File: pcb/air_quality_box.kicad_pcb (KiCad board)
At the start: 2 copper layers, 10 parts, among them J1 MH-Z19B, J2 Conn_01x06_Female, J3 Conn_01x05_Male, J4 Conn_01x09_Female, SW1 SW_SPDT, U1 NodeMCU_ESP8266

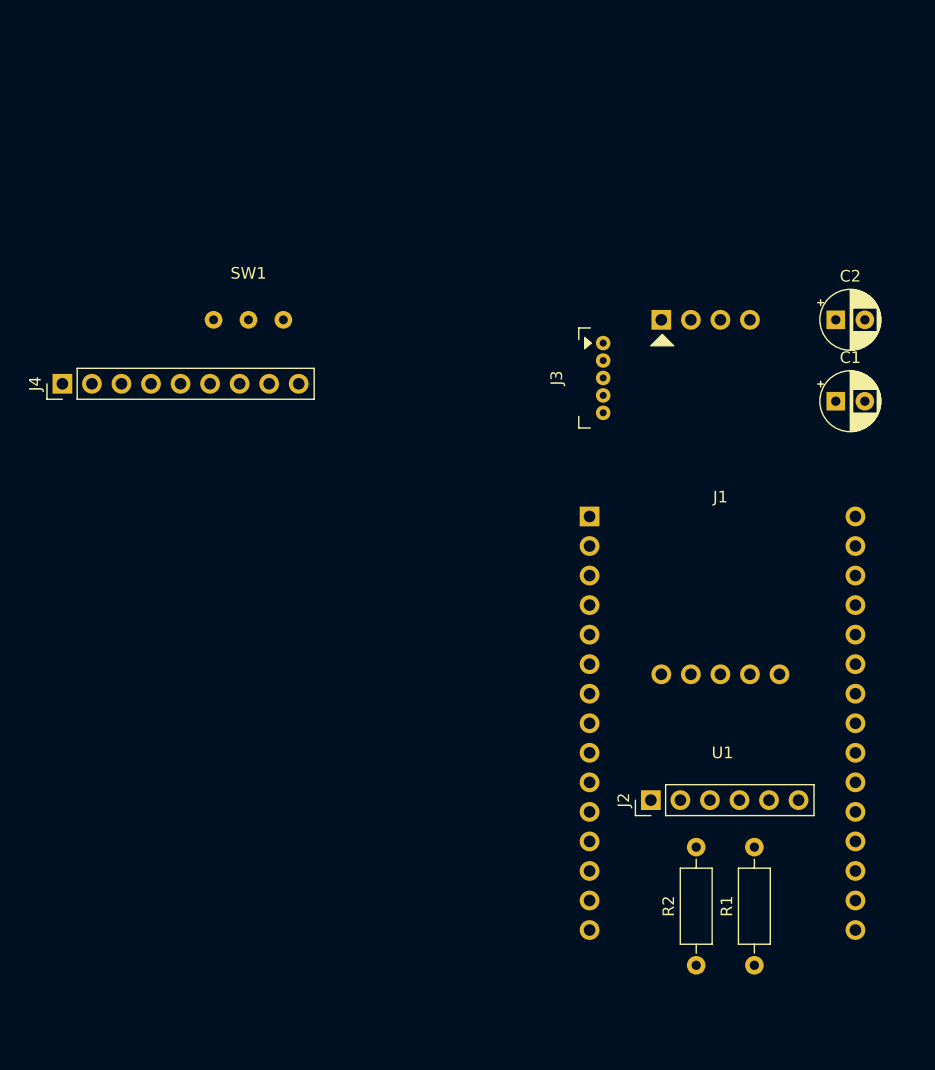
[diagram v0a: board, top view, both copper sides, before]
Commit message: Create basic board layout
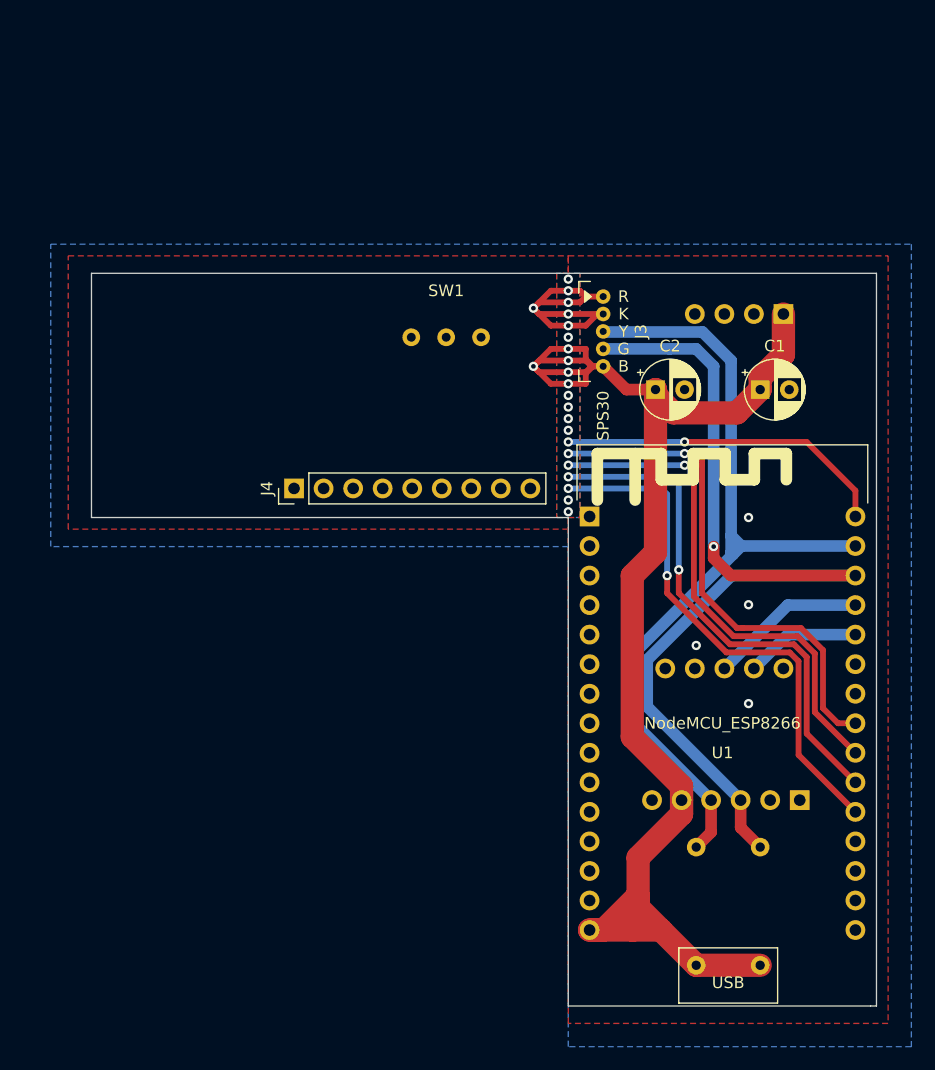
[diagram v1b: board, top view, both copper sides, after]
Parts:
- J1, R1, R2: moved to B.Cu
- J2: value Conn_01x06_Female -> BME680; moved to B.Cu
- J3: value Conn_01x05_Male -> SPS30
- J4: value Conn_01x09_Female -> ST7565
- moved J4 21.9 mm to (115.9, 62.0)
- moved SW1 17.1 mm to (129.0, 49.0)
- moved C2 16.6 mm to (147.0, 53.5)
- moved J2 12.8 mm to (159.4, 88.8)
- moved C1 6.58 mm to (156.0, 53.5)
- moved R2 5.50 mm to (156.0, 103.0)
- moved R1 5.00 mm to (150.5, 103.0)
- moved J3 4.00 mm to (142.5, 48.5)
- moved J1 0.60 mm to (152.9, 62.2), turned to 180 degrees
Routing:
- net +5V: track 0.00 -> 126.0 mm, vias 0 -> 5
- net I2C_SDA: track 0.00 -> 80.5 mm, vias 0 -> 1
- net I2C_SCL: track 0.00 -> 72.9 mm
- net LCD_CS: track 0.00 -> 45.9 mm, vias 0 -> 2
- net LCD_DC: track 0.00 -> 45.0 mm, vias 0 -> 2
- net SPI_MOSI: track 0.00 -> 44.3 mm, vias 0 -> 2
- net SPI_SCL: track 0.00 -> 44.0 mm, vias 0 -> 2
- net LCD_RST: track 0.00 -> 28.6 mm, vias 0 -> 2
- net GND: track 0.00 -> 25.0 mm, vias 0 -> 9
- net UART_1_RX: track 0.00 -> 13.5 mm
- net UART_1_TX: track 0.00 -> 9.94 mm
- net (no net): vias 0 -> 8
- added copper zone on B.Cu, net GND
- added copper zone on F.Cu, net GND
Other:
- board outline added: 67.5 x 63 mm
- board text added: "B"
- board text added: "G"
- board text added: "K"
- board text added: "R"
- board text added: "USB"
- board text added: "Y"

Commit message: Position the LCD in the center of the board
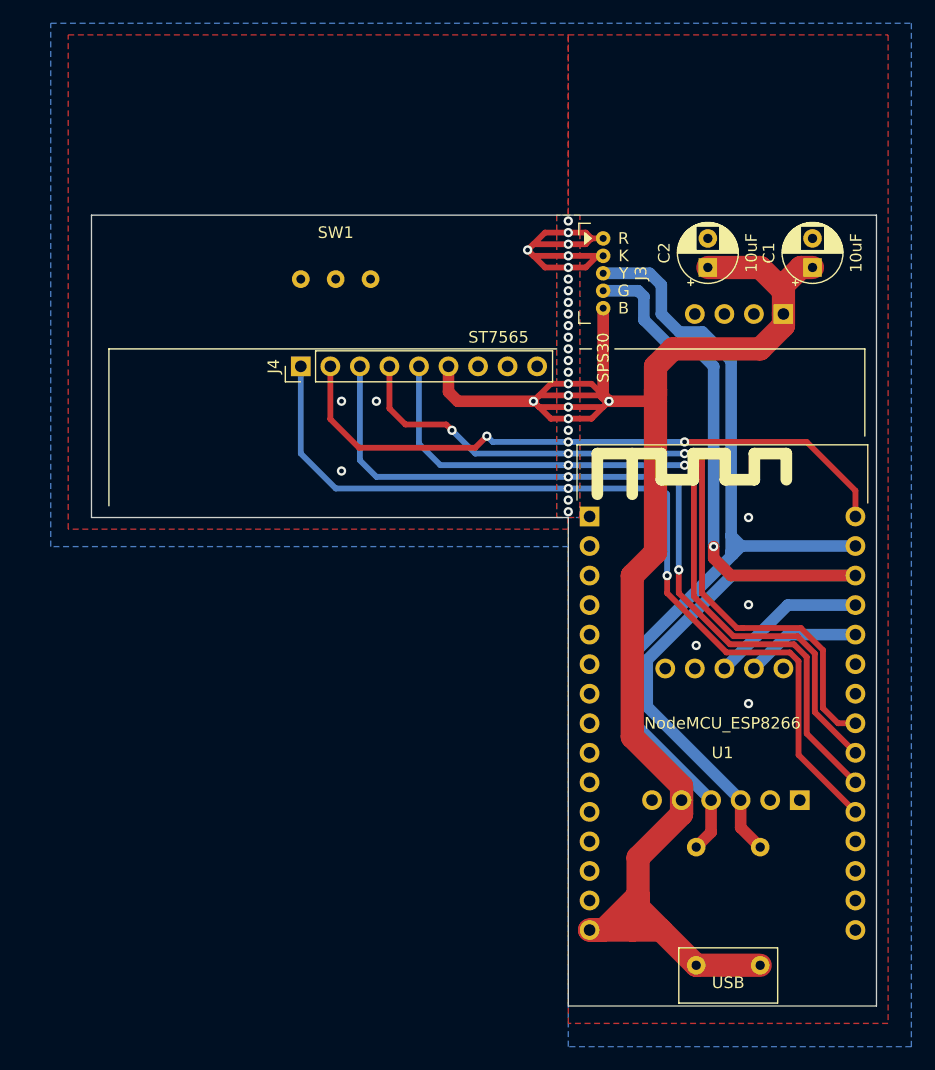
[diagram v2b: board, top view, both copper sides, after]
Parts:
- moved C1 11.4 mm to (160.5, 43.0), turned to 90 degrees
- moved C2 11.4 mm to (151.5, 43.0), turned to 90 degrees
- moved SW1 10.7 mm to (119.5, 44.0)
- moved J4 10.5 mm to (116.5, 51.5)
- moved J3 5.00 mm to (142.5, 43.5)
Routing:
- net LCD_CS: track 45.9 -> 77.7 mm
- net +5V: track 126.0 -> 155.4 mm, vias 5 -> 6
- net LCD_RST: track 28.6 -> 55.3 mm, vias 2 -> 3
- net LCD_DC: track 45.0 -> 71.6 mm
- net SPI_SCL: track 44.0 -> 64.6 mm, vias 2 -> 3
- net SPI_MOSI: track 44.3 -> 64.6 mm
- net I2C_SCL: track 72.9 -> 76.4 mm
- net I2C_SDA: track 80.5 -> 83.7 mm
- net GND: track 25.0 -> 27.0 mm, vias 9 -> 12
- net (no net): vias 8 -> 13
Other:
- board size 67.5 x 63 mm -> 67.5 x 68 mm

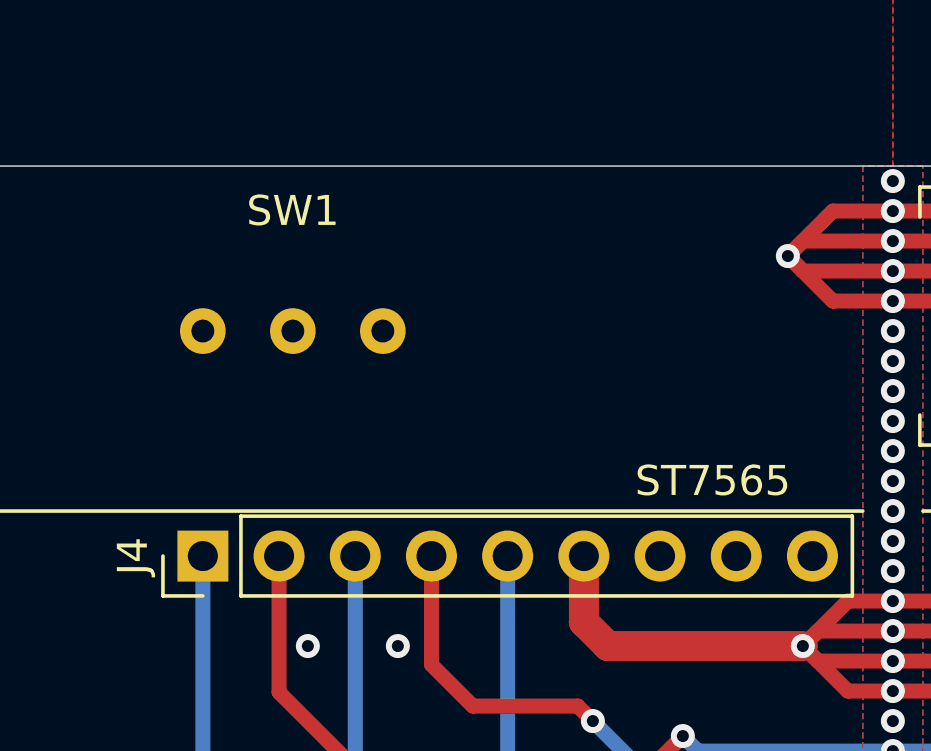
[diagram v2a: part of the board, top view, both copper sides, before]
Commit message: Add JCL order number location to board
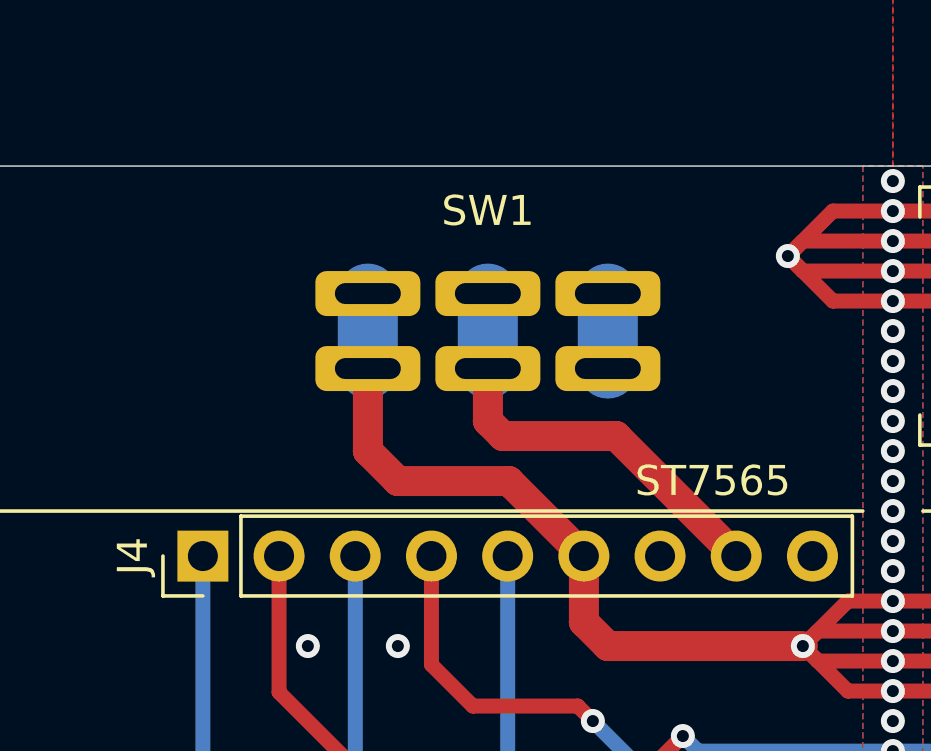
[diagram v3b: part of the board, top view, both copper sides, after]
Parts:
- moved SW1 6.50 mm to (126.0, 44.0)
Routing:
- net Net-(J4-Pad8): track 0.00 -> 14.4 mm
- net +5V: track 155.4 -> 169.3 mm
- net Net-(SW1-Pad1): track 0.00 -> 2.50 mm
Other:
- board text added: "JLCJLCJLCJLC"
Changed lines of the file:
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@@
   (general
     (thickness 1.6)
-    (drawings 58)
-    (tracks 217)
+    (drawings 59)
+    (tracks 228)
     (zones 0)
     (modules 10)
@@
   )
   (setup
-    (last_trace_width 0.5)
+    (last_trace_width 2)
     (user_trace_width 0.5)
     (user_trace_width 1)
@@
       (outputformat 1)
       (mirror false)
-      (drillshape 1)
+      (drillshape 0)
       (scaleselection 1)
       (outputdirectory ""))
@@
     (add_net UART_1_RX)
     (add_net UART_1_TX)
+  )
+  (module air_quality_box:switch (layer F.Cu)
+    (at 126 44 180)
+    (fp_text reference SW1 (at 0 4) (layer F.SilkS)
+      (effects (font (size 1 1) (thickness 0.15)))
+    )
+    (fp_text value SW_SPDT (at 0 -5) (layer F.Fab)
+      (effects (font (size 1 1) (thickness 0.15)))
+    )
+    (fp_line (start -8 0) (end -8 -4) (layer F.Fab) (width 0.12))
+    (fp_line (start -8 -4) (end 8 -4) (layer F.Fab) (width 0.12))
+    (fp_line (start 8 -4) (end 8 4) (layer F.Fab) (width 0.12))
+    (fp_line (start 8 4) (end -8 4) (layer F.Fab) (width 0.12))
+    (fp_line (start -8 4) (end -8 0) (layer F.Fab) (width 0.12))
+    (fp_line (start -8 -4) (end -12 -4) (layer F.Fab) (width 0.12))
+    (fp_line (start -12 -4) (end -12 4) (layer F.Fab) (width 0.12))
+    (fp_line (start -12 4) (end -8 4) (layer F.Fab) (width 0.12))
+    (fp_line (start 8 4) (end 12 4) (layer F.Fab) (width 0.12))
+    (fp_line (start 12 4) (end 12 -4) (layer F.Fab) (width 0.12))
+    (fp_line (start 12 -4) (end 8 -4) (layer F.Fab) (width 0.12))
+    (pad 3 thru_hole roundrect (at 4 1.25 180) (size 3.5 1.5) (drill oval 2.2 0.7) (layers *.Cu *.Mask) (roundrect_rratio 0.25)
+      (net 1 +5V))
+    (pad 2 thru_hole roundrect (at 0 1.25 180) (size 3.5 1.5) (drill oval 2.2 0.7) (layers *.Cu *.Mask) (roundrect_rratio 0.25)
+      (net 19 "Net-(J4-Pad8)"))
+    (pad 1 thru_hole roundrect (at -4 1.25 180) (size 3.5 1.5) (drill oval 2.2 0.7) (layers *.Cu *.Mask) (roundrect_rratio 0.25)
+      (net 20 "Net-(SW1-Pad1)"))
+    (pad 3 thru_hole roundrect (at 4 -1.25 180) (size 3.5 1.5) (drill oval 2.2 0.7) (layers *.Cu *.Mask) (roundrect_rratio 0.25)
+      (net 1 +5V))
+    (pad 2 thru_hole roundrect (at 0 -1.25 180) (size 3.5 1.5) (drill oval 2.2 0.7) (layers *.Cu *.Mask) (roundrect_rratio 0.25)
+      (net 19 "Net-(J4-Pad8)"))
+    (pad 1 thru_hole roundrect (at -4 -1.25 180) (size 3.5 1.5) (drill oval 2.2 0.7) (layers *.Cu *.Mask) (roundrect_rratio 0.25)
+      (net 20 "Net-(SW1-Pad1)"))
   )
   (module air_quality_box:ZH_1.5mm_5P (layer F.Cu)
@@
     )
   )
-  (module air_quality_box:switch (layer F.Cu)
-    (at 119.5 44 180)
-    (fp_text reference SW1 (at 0 4) (layer F.SilkS)
-      (effects (font (size 1 1) (thickness 0.15)))
-    )
-    (fp_text value SW_SPDT (at 0 -5) (layer F.Fab)
-      (effects (font (size 1 1) (thickness 0.15)))
-    )
-    (pad 1 thru_hole circle (at -3 0 180) (size 1.524 1.524) (drill 0.762) (layers *.Cu *.Mask)
-      (net 20 "Net-(SW1-Pad1)"))
-    (pad 2 thru_hole circle (at 0 0 180) (size 1.524 1.524) (drill 0.762) (layers *.Cu *.Mask)
-      (net 19 "Net-(J4-Pad8)"))
-    (pad 3 thru_hole circle (at 3 0 180) (size 1.524 1.524) (drill 0.762) (layers *.Cu *.Mask)
-      (net 1 +5V))
-  )
   (module air_quality_box:NodeMCU_ESP8266 (layer F.Cu)
     (at 152.760001 82.190001)
@@
     (pad 30 thru_hole circle (at 11.43 17.78) (size 1.7 1.7) (drill 1) (layers *.Cu *.Mask)
       (net 36 "Net-(U1-Pad30)"))
+  )
+  (gr_text JLCJLCJLCJLC (at 105 63) (layer B.SilkS)
+    (effects (font (size 1 1) (thickness 0.15)) (justify mirror))
   )
   (gr_line (start 165 50) (end 165 57.5) (layer F.SilkS) (width 0.12))
@@
   (segment (start 142.5 54) (end 143 54.5) (width 1) (layer F.Cu) (net 1))
   (segment (start 142.5 46.5) (end 142.5 54) (width 1) (layer F.Cu) (net 1))
+  (segment (start 129.2 51.5) (end 126.7 49) (width 1) (layer F.Cu) (net 1))
+  (segment (start 126.7 49) (end 123 49) (width 1) (layer F.Cu) (net 1))
+  (segment (start 122 48) (end 122 45.25) (width 1) (layer F.Cu) (net 1))
+  (segment (start 123 49) (end 122 48) (width 1) (layer F.Cu) (net 1))
+  (segment (start 122 42.75) (end 122 45.25) (width 2) (layer B.Cu) (net 1))
   (segment (start 139.5 40) (end 141 40) (width 0.5) (layer F.Cu) (net 2))
   (segment (start 141.5 40.5) (end 142.5 40.5) (width 0.5) (layer F.Cu) (net 2))
@@
   (segment (start 126.66 58.16) (end 126.66 51.5) (width 0.5) (layer B.Cu) (net 18))
   (segment (start 128.5 60) (end 126.66 58.16) (width 0.5) (layer B.Cu) (net 18))
+  (segment (start 134.28 51.5) (end 130.28 47.5) (width 1) (layer F.Cu) (net 19))
+  (segment (start 130.28 47.5) (end 126.5 47.5) (width 1) (layer F.Cu) (net 19))
+  (segment (start 126 47) (end 126 45.25) (width 1) (layer F.Cu) (net 19))
+  (segment (start 126.5 47.5) (end 126 47) (width 1) (layer F.Cu) (net 19))
+  (segment (start 126 42.75) (end 126 45.25) (width 2) (layer B.Cu) (net 19))
+  (segment (start 130 42.75) (end 130 45.25) (width 2) (layer B.Cu) (net 20))
   (zone (net 2) (net_name GND) (layer F.Cu) (hatch edge 0.508)
     (connect_pads (clearance 0.508))

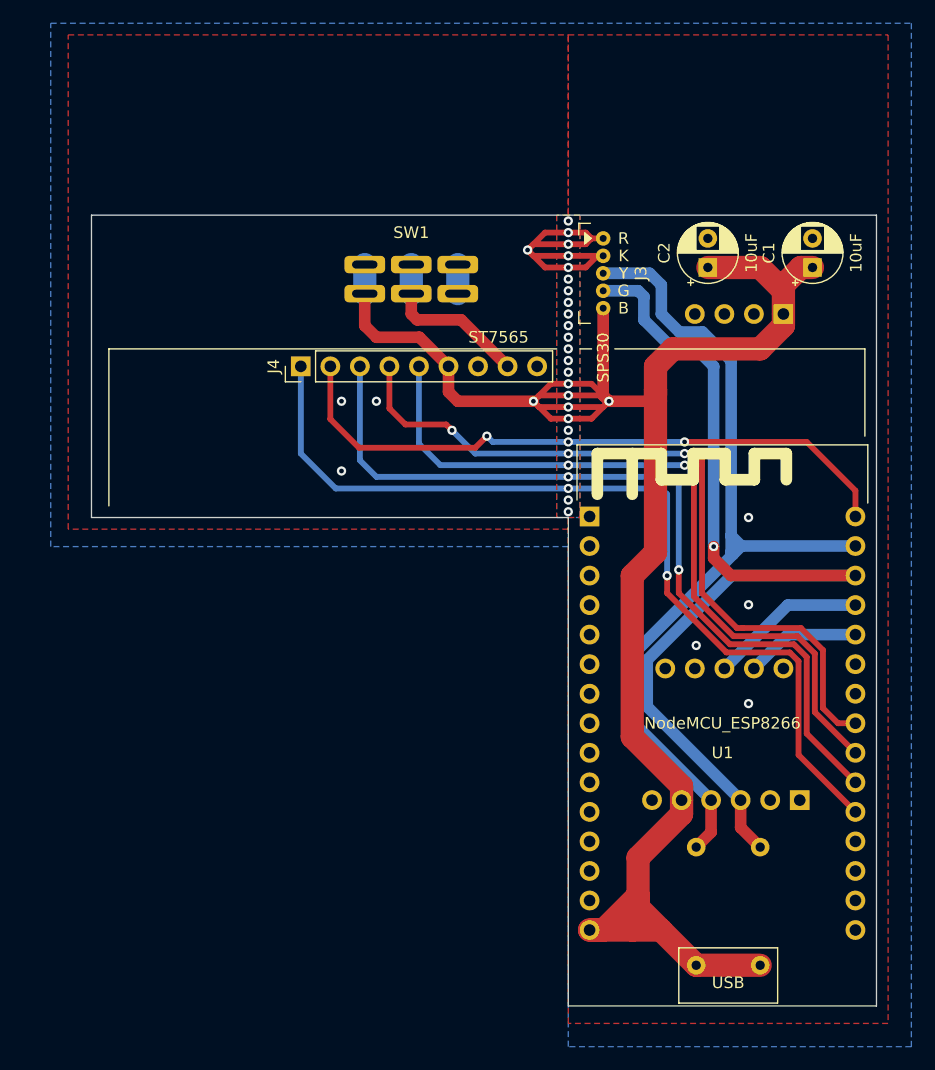
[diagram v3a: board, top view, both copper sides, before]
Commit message: Swap VCC and GNC pins on BME680
This mistake nearly cost me the sensor. To my luck only the regulator
released the magick smoke. After replacing the regulator the sensor
started working again.

Also, the screen diode draws a lot of current. Through experimentation I
figured out that it's bright enough with just 15mA of current. So I
added a 440 Ohm load in series with the backlight to limit the current
to about that value. This made also all sensor readings more stable, as
the MH-Z19 sensor draws up-to 100mA which brown-outs the MCU and other
sensors. Lowering the LCD current draw fixed that problem as well.
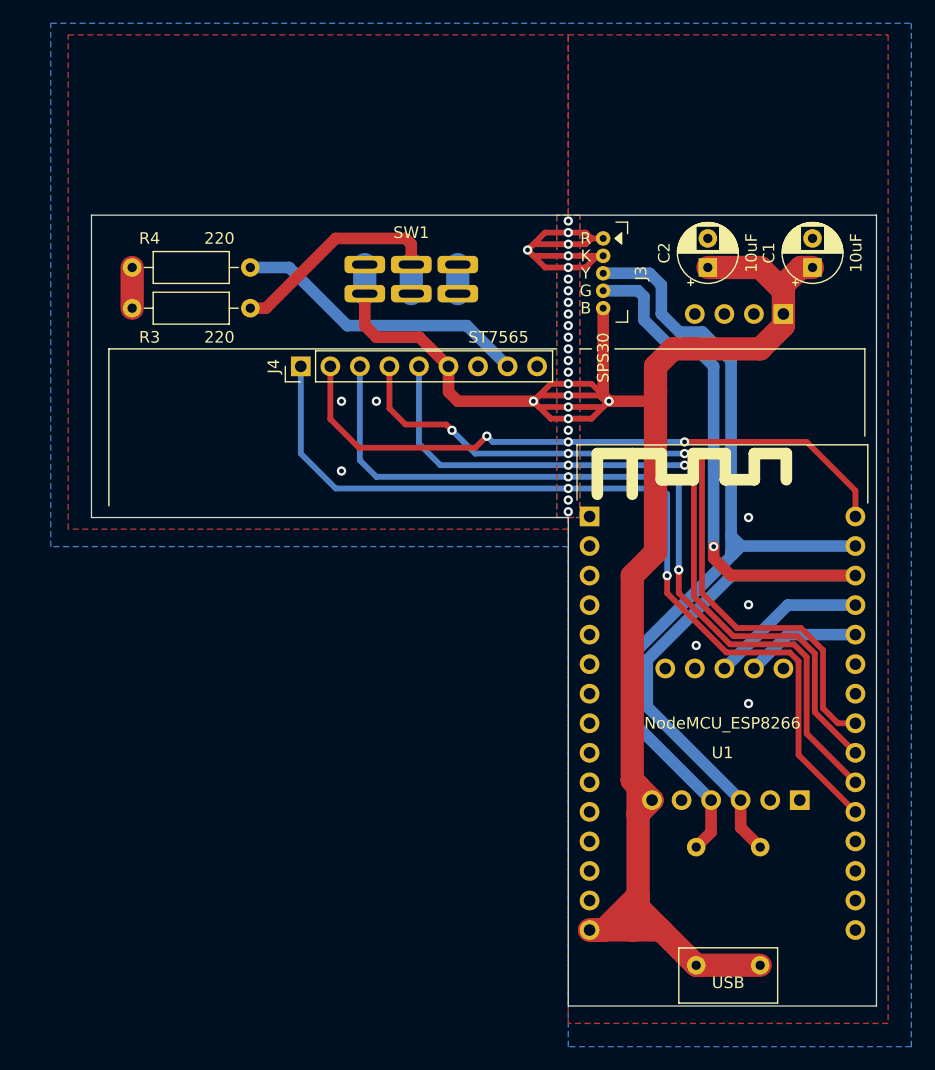
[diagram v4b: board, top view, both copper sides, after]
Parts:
- added R3: 220, Resistor_THT:R_Axial_DIN0207_L6.3mm_D2.5mm_P10.16mm_Horizontal, F.Cu at (102.0, 46.5)
- added R4: 220, Resistor_THT:R_Axial_DIN0207_L6.3mm_D2.5mm_P10.16mm_Horizontal, F.Cu at (112.2, 43.0)
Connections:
- J2 pad 5: +5V -> GND
- J2 pad 6: GND -> +5V
- SW1 pad 2: Net-(J4-Pad8) -> Net-(R3-Pad2)
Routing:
- net Net-(R3-Pad2): track 0.00 -> 20.8 mm
- net Net-(J4-Pad8): track 14.4 -> 25.6 mm
- net Net-(R3-Pad1): track 0.00 -> 3.50 mm
- net +5V: track 169.3 -> 170.3 mm
